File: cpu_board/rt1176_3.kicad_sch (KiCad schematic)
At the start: 19 parts

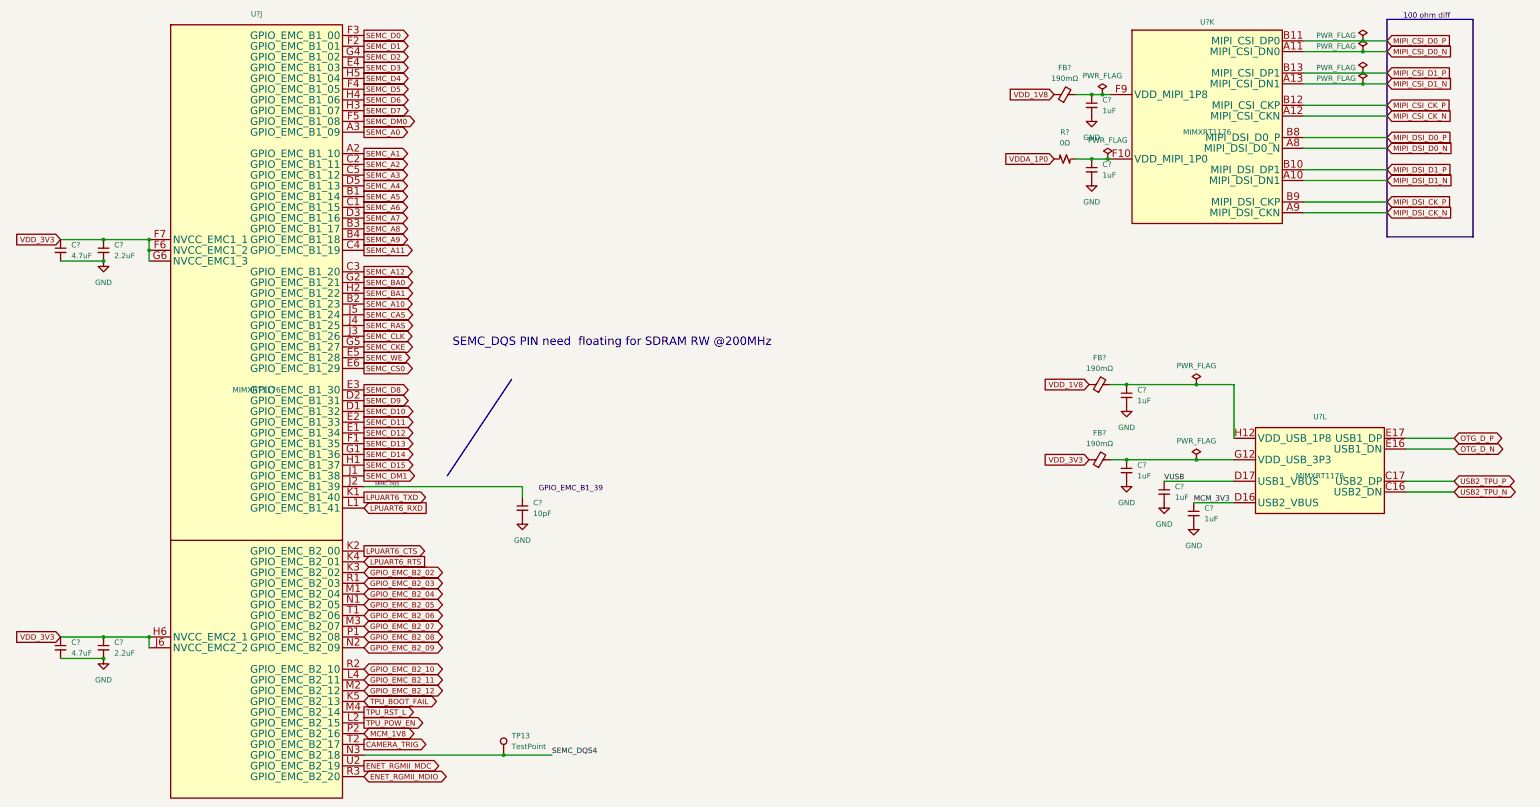
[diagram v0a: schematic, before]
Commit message: clean up board2board connector and organize TODOs
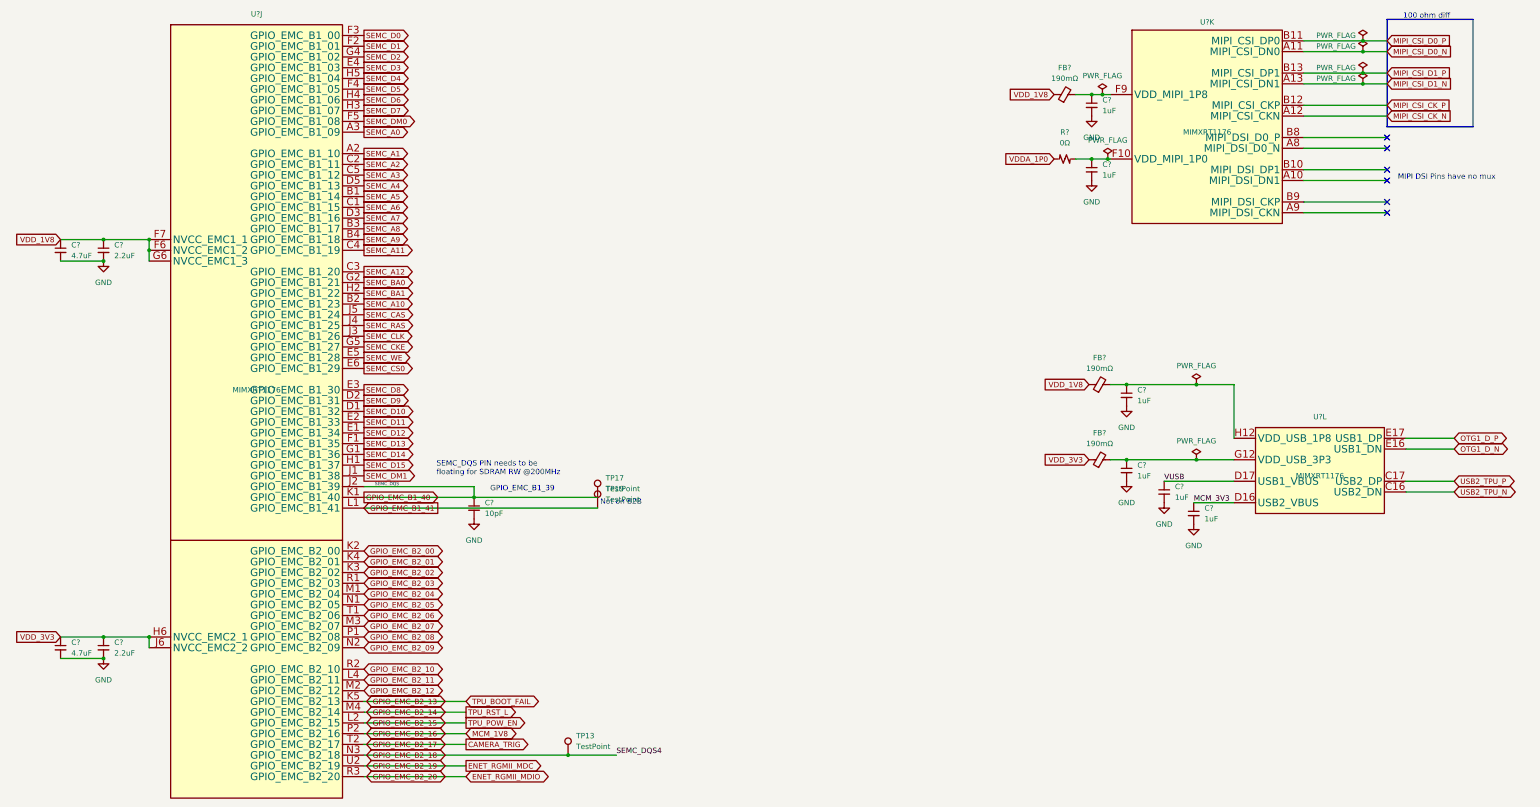
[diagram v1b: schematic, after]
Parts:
- added TP17, TP19: TestPoint, TestPoint:TestPoint_Pad_1.5x1.5mm, symbol Connector:TestPoint
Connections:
- net LPUART6_TXD is gone; now on net GPIO_EMC_B1_40: U?.K1 (GPIO_EMC_B1_40)
- net VDD_1V8: now also C?.1, C?.1, U?.F6 (NVCC_EMC1_2), U?.F7 (NVCC_EMC1_1), U?.G6 (NVCC_EMC1_3)
- net VDD_3V3: no longer C?.1, C?.1, U?.F6 (NVCC_EMC1_2), U?.F7 (NVCC_EMC1_1), U?.G6 (NVCC_EMC1_3)
- net GPIO_EMC_B1_40: now reaches C?.1, U?.J2 (GPIO_EMC_B1_39)
- net GPIO_EMC_B1_40: now also TP17.1
- net LPUART6_CTS renamed GPIO_EMC_B2_00
- net LPUART6_RTS renamed GPIO_EMC_B2_01
- net LPUART6_RXD renamed GPIO_EMC_B1_41
- net GPIO_EMC_B1_41: now also TP19.1
- net MCM_1V8 renamed GPIO_EMC_B2_16
- net MIPI_DSI_CK_N: no longer names the net of U?.A9 (MIPI_DSI_CKN)
- net MIPI_DSI_CK_P: no longer names the net of U?.B9 (MIPI_DSI_CKP)
- net MIPI_DSI_D0_N: no longer names the net of U?.A8 (MIPI_DSI_D0_N)
- net MIPI_DSI_D0_P: no longer names the net of U?.B8 (MIPI_DSI_D0_P)
- net MIPI_DSI_D1_N: no longer names the net of U?.A10 (MIPI_DSI_DN1)
- net MIPI_DSI_D1_P: no longer names the net of U?.B10 (MIPI_DSI_DP1)
- net OTG_D_N renamed OTG1_D_N
- net OTG_D_P renamed OTG1_D_P
- net SEMC_DQS4 renamed GPIO_EMC_B2_18
- net TPU_BOOT_FAIL renamed GPIO_EMC_B2_13
- net TPU_POW_EN renamed GPIO_EMC_B2_15
- net TPU_RST_L renamed GPIO_EMC_B2_14
- no-connect marks 0 -> 6
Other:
- note added: "MIPI DSI Pins have no mux"
- note added: "Not on B2B"
- note added: "SEMC_DQS PIN needs to be floating for SDRAM RW @200MHz"
- note removed: "SEMC_DQS PIN need floating for SDRAM RW @200MHz"
- moved on the sheet: C?, TP13

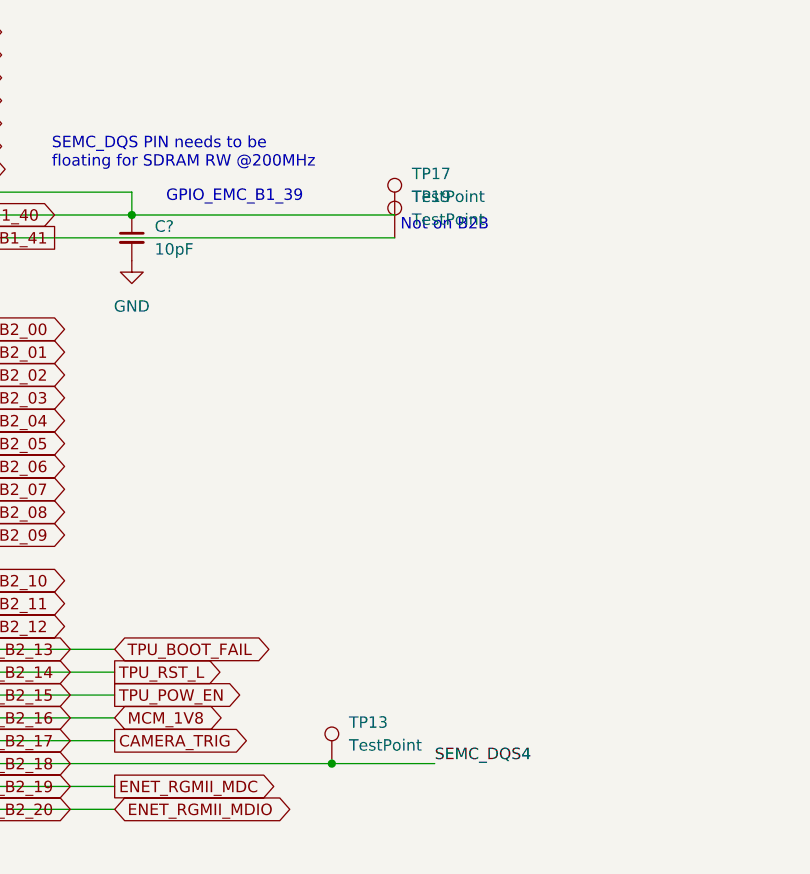
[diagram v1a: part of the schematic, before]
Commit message: route most of power distribution
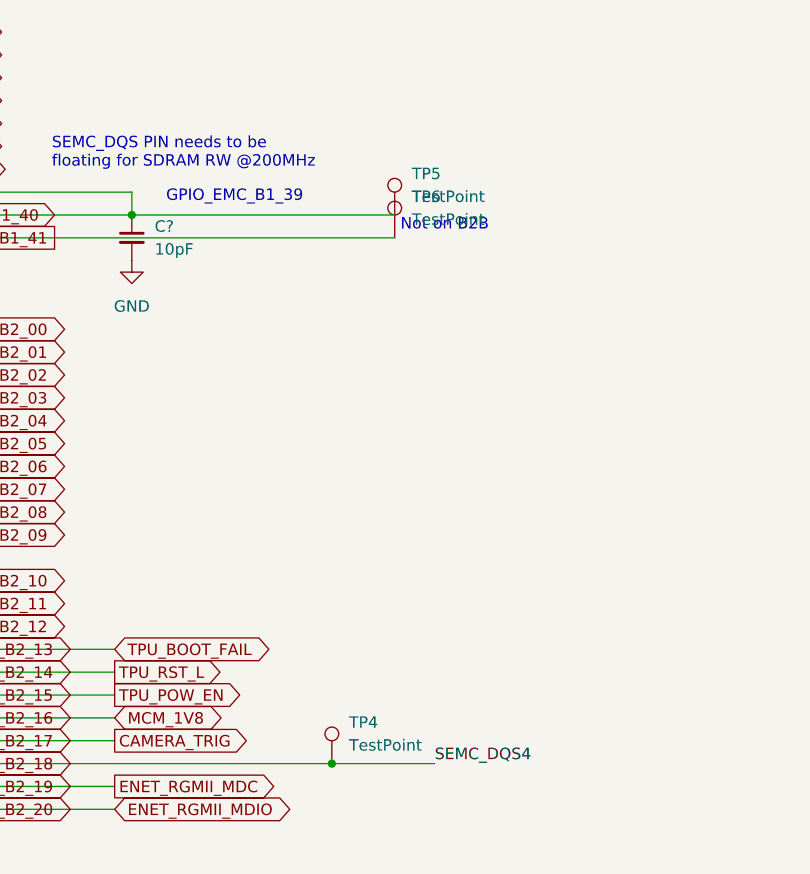
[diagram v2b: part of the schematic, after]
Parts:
- TP4: renamed from TP13; footprint TestPoint:TestPoint_Pad_1.5x1.5mm -> TestPoint:TestPoint_Pad_1.0x1.0mm; JLCPCB P/N (none) -> C221678
- TP5: renamed from TP17; footprint TestPoint:TestPoint_Pad_1.5x1.5mm -> TestPoint:TestPoint_Pad_1.0x1.0mm; JLCPCB P/N (none) -> C221678
- TP6: renamed from TP19; footprint TestPoint:TestPoint_Pad_1.5x1.5mm -> TestPoint:TestPoint_Pad_1.0x1.0mm; JLCPCB P/N (none) -> C221678

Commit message: floorplan complete
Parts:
- removed C?: 1uF, Capacitor_SMD:C_0402_1005Metric, symbol Device:C_Small
- removed C?: 10pF, Capacitor_SMD:C_0402_1005Metric, symbol Device:C_Small
- removed R?: 0Ω, Resistor_SMD:R_0402_1005Metric, symbol Device:R_Small_US
- removed TP4, TP5, TP6: TestPoint, TestPoint:TestPoint_Pad_1.0x1.0mm, symbol Connector:TestPoint
- added C?: 10pF, Capacitor_SMD:C_0402_1005Metric, symbol Device:C_Small
- added R?: 10kΩ, Resistor_SMD:R_0402_1005Metric, symbol Device:R_Small_US
- FB? (x3): footprint adcs:L0402_H0.55MM -> Inductor_SMD:L_0402_1005Metric
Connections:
- net GND: now also C?.2, R?.1
- net GPIO_EMC_B1_40: no longer U?.J2 (GPIO_EMC_B1_39)
- net VDD_USB_3P3: now reaches C?.1, FB?.2, U?.G12 (VDD_USB_3P3)
- net VDD_USB_1P8: now reaches C?.1, FB?.2, U?.H12 (VDD_USB_1P8)
- net VDD_MIPI_1P0: now reaches U?.F10 (VDD_MIPI_1P0)
- net VDD_MIPI_1P0: now also R?.2
- new net SEMC_DQS: C?.1, U?.J2 (GPIO_EMC_B1_39)
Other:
- note added: "Per HDUG, 10k resistor to ground recommended when not in use"
- note removed: "GPIO_EMC_B1_39"
- note removed: "Not on B2B"
- note removed: "SEMC_DQS"

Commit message: add models and power diagram
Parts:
- U? (x3): footprint adcs:BGA289C80P17X17_1400X14000X152 -> adcs:U_MIMXRT1176DVMAA_NXP
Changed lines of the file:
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@@
       (effects (font (size 1.27 1.27)))
     )
-    (property "Footprint" "adcs:BGA289C80P17X17_1400X14000X152" (at 314.96 83.185 0)
+    (property "Footprint" "adcs:U_MIMXRT1176DVMAA_NXP" (at 314.96 83.185 0)
       (effects (font (size 1.27 1.27)) hide)
     )
@@
     (property "Footprint (for JLCPCB)" "" (at 314.96 81.915 0)
       (effects (font (size 1.27 1.27)) hide)
+    )
+    (property "DigiKey Part Number" "" (at 314.96 81.915 0)
+      (effects (font (size 1.27 1.27)) hide)
+    )
+    (property "Tolerance" "" (at 314.96 81.915 0)
+      (effects (font (size 1.27 1.27)))
+    )
+    (property "Power Rating" "" (at 314.96 81.915 0)
+      (effects (font (size 1.27 1.27)))
     )
     (pin "L9")
@@
       (effects (font (size 1.27 1.27)))
     )
-    (property "Footprint" "adcs:BGA289C80P17X17_1400X14000X152" (at 90.17 144.145 0)
+    (property "Footprint" "adcs:U_MIMXRT1176DVMAA_NXP" (at 90.17 144.145 0)
       (effects (font (size 1.27 1.27)) hide)
     )
@@
     (property "Footprint (for JLCPCB)" "" (at 90.17 142.875 0)
       (effects (font (size 1.27 1.27)) hide)
+    )
+    (property "DigiKey Part Number" "" (at 90.17 142.875 0)
+      (effects (font (size 1.27 1.27)) hide)
+    )
+    (property "Tolerance" "" (at 90.17 142.875 0)
+      (effects (font (size 1.27 1.27)))
+    )
+    (property "Power Rating" "" (at 90.17 142.875 0)
+      (effects (font (size 1.27 1.27)))
     )
     (pin "L9")
@@
       (effects (font (size 1.27 1.27)))
     )
-    (property "Footprint" "adcs:BGA289C80P17X17_1400X14000X152" (at 341.63 164.465 0)
+    (property "Footprint" "adcs:U_MIMXRT1176DVMAA_NXP" (at 341.63 164.465 0)
       (effects (font (size 1.27 1.27)) hide)
     )
@@
       (effects (font (size 1.27 1.27)) hide)
     )
+    (property "DigiKey Part Number" "" (at 341.63 163.195 0)
+      (effects (font (size 1.27 1.27)) hide)
+    )
+    (property "Tolerance" "" (at 341.63 163.195 0)
+      (effects (font (size 1.27 1.27)))
+    )
+    (property "Power Rating" "" (at 341.63 163.195 0)
+      (effects (font (size 1.27 1.27)))
+    )
     (pin "L9")

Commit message: continue work on fanout
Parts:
- removed FB? (x2): 190mΩ, Inductor_SMD:L_0402_1005Metric, symbol Device:FerriteBead_Small
- C? (x9): footprint Capacitor_SMD:C_0402_1005Metric -> adcs:Perfect_0201
- C?: footprint Capacitor_SMD:C_0402_1005Metric -> adcs:Perfect_0402
- FB?: footprint Inductor_SMD:L_0402_1005Metric -> adcs:Perfect_0402
- R?: footprint Resistor_SMD:R_0402_1005Metric -> adcs:Perfect_0201
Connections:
- net VDD_USB_1P8 is gone; now on net VDD_1V8: C?.1, U?.H12 (VDD_USB_1P8)
- net VDD_USB_3P3 is gone; now on net VDD_3V3: C?.1, U?.G12 (VDD_USB_3P3)
- net MIPI_CSI_CK_N: no longer names the net of U?.A12 (MIPI_CSI_CKN)
- net MIPI_CSI_CK_P: no longer names the net of U?.B12 (MIPI_CSI_CKP)
- net MIPI_CSI_D0_N: no longer names the net of U?.A11 (MIPI_CSI_DN0)
- net MIPI_CSI_D0_P: no longer names the net of U?.B11 (MIPI_CSI_DP0)
- net MIPI_CSI_D1_N: no longer names the net of U?.A13 (MIPI_CSI_DN1)
- net MIPI_CSI_D1_P: no longer names the net of U?.B13 (MIPI_CSI_DP1)
- net USB2_TPU_N: no longer names the net of U?.C16 (USB2_DN)
- net USB2_TPU_P: no longer names the net of U?.C17 (USB2_DP)
- no-connect marks 6 -> 14
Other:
- note added: "Do I need to power this if we are not using the OTGs?"
- note added: "MIPI_CSI_CK_N"
- note added: "MIPI_CSI_CK_P"
- note added: "MIPI_CSI_D0_N"
- note added: "MIPI_CSI_D0_P"
- note added: "MIPI_CSI_D1_N"
- note added: "MIPI_CSI_D1_P"
- note added: "Removed ferrite beads here!"

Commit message: clean up silkscreen
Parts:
- C? (x9), R?: Footprint (for JLCPCB) 0402 -> 0201
- FB?: Footprint (for JLCPCB) (none) -> 0401
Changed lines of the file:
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@@
       (effects (font (size 1.27 1.27)) hide)
     )
-    (property "Footprint (for JLCPCB)" "0402" (at 43.815 111.125 0)
+    (property "Footprint (for JLCPCB)" "0201" (at 43.815 111.125 0)
       (effects (font (size 1.27 1.27)) hide)
     )
@@
       (effects (font (size 1.27 1.27)) hide)
     )
-    (property "Footprint (for JLCPCB)" "0402" (at 43.815 205.105 0)
+    (property "Footprint (for JLCPCB)" "0201" (at 43.815 205.105 0)
       (effects (font (size 1.27 1.27)) hide)
     )
@@
       (effects (font (size 1.27 1.27)) hide)
     )
-    (property "Footprint (for JLCPCB)" "0402" (at 177.165 170.18 0)
+    (property "Footprint (for JLCPCB)" "0201" (at 177.165 170.18 0)
       (effects (font (size 1.27 1.27)) hide)
     )
@@
       (effects (font (size 1.27 1.27)) hide)
     )
-    (property "Datasheet" "~" (at 281.305 74.295 0)
+    (property "Datasheet" "" (at 281.305 74.295 0)
       (effects (font (size 1.27 1.27)) hide)
     )
@@
       (effects (font (size 1.27 1.27)) hide)
     )
-    (property "Footprint (for JLCPCB)" "" (at 281.305 74.295 0)
+    (property "Footprint (for JLCPCB)" "0401" (at 281.305 74.295 0)
       (effects (font (size 1.27 1.27)) hide)
     )
@@
       (effects (font (size 1.27 1.27)) hide)
     )
-    (property "Footprint (for JLCPCB)" "0402" (at 287.655 76.835 0)
+    (property "Footprint (for JLCPCB)" "0201" (at 287.655 76.835 0)
       (effects (font (size 1.27 1.27)) hide)
     )
@@
       (effects (font (size 1.27 1.27)) hide)
     )
-    (property "Datasheet" "~" (at 53.975 111.125 0)
+    (property "Datasheet" "" (at 53.975 111.125 0)
       (effects (font (size 1.27 1.27)) hide)
     )
@@
       (effects (font (size 1.27 1.27)) hide)
     )
-    (property "Footprint (for JLCPCB)" "0402" (at 53.975 111.125 0)
+    (property "Footprint (for JLCPCB)" "0201" (at 53.975 111.125 0)
       (effects (font (size 1.27 1.27)) hide)
     )
@@
       (effects (font (size 1.27 1.27)) hide)
     )
-    (property "Footprint (for JLCPCB)" "0402" (at 311.785 173.355 0)
+    (property "Footprint (for JLCPCB)" "0201" (at 311.785 173.355 0)
       (effects (font (size 1.27 1.27)) hide)
     )
@@
       (effects (font (size 1.27 1.27)) hide)
     )
-    (property "Datasheet" "~" (at 53.975 205.105 0)
+    (property "Datasheet" "" (at 53.975 205.105 0)
       (effects (font (size 1.27 1.27)) hide)
     )
@@
       (effects (font (size 1.27 1.27)) hide)
     )
-    (property "Footprint (for JLCPCB)" "0402" (at 53.975 205.105 0)
+    (property "Footprint (for JLCPCB)" "0201" (at 53.975 205.105 0)
       (effects (font (size 1.27 1.27)) hide)
     )
@@
       (effects (font (size 1.27 1.27)) hide)
     )
-    (property "Footprint (for JLCPCB)" "0402" (at 291.465 92.075 0)
+    (property "Footprint (for JLCPCB)" "0201" (at 291.465 92.075 0)
       (effects (font (size 1.27 1.27)) hide)
     )
@@
       (effects (font (size 1.27 1.27)) hide)
     )
-    (property "Footprint (for JLCPCB)" "0402" (at 295.91 145.415 0)
+    (property "Footprint (for JLCPCB)" "0201" (at 295.91 145.415 0)
       (effects (font (size 1.27 1.27)) hide)
     )
@@
       (effects (font (size 1.27 1.27)) hide)
     )
-    (property "Footprint (for JLCPCB)" "0402" (at 295.91 163.195 0)
-      (effects (font (size 1.27 1.27)) hide)
-    )
+    (property "Footprint (for JLCPCB)" "0201" (at 295.91 163.195 0)
+      (effects (font (size 1.27 1.27)) hide)
+    )

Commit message: soldermander 1.0 ready for review
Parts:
- C? (x2): Voltage Rating (none) -> 6.3V
- C? (x2): Voltage Rating (none) -> 50V
- C? (x6): Voltage Rating (none) -> 10V
- R?: JLCPCB P/N (none) -> C3152014
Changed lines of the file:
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@@
       (effects (font (size 1.27 1.27)))
+    )
+    (property "Voltage Rating" "6.3V" (at 43.815 111.125 0)
+      (effects (font (size 1.27 1.27)) hide)
     )
     (pin "1")
@@
       (effects (font (size 1.27 1.27)))
     )
+    (property "Voltage Rating" "6.3V" (at 43.815 205.105 0)
+      (effects (font (size 1.27 1.27)) hide)
+    )
     (pin "1")
     (pin "2")
@@
       (effects (font (size 1.27 1.27)) hide)
     )
+    (property "Voltage Rating" "50V" (at 177.165 170.18 0)
+      (effects (font (size 1.27 1.27)) hide)
+    )
     (pin "1")
     (pin "2")
@@
       (effects (font (size 1.27 1.27)) hide)
     )
+    (property "Voltage Rating" "10V" (at 287.655 76.835 0)
+      (effects (font (size 1.27 1.27)) hide)
+    )
     (pin "1")
     (pin "2")
@@
       (effects (font (size 1.27 1.27)) hide)
     )
+    (property "Voltage Rating" "10V" (at 53.975 111.125 0)
+      (effects (font (size 1.27 1.27)) hide)
+    )
     (pin "1")
     (pin "2")
@@
       (effects (font (size 1.27 1.27)) hide)
     )
+    (property "Voltage Rating" "10V" (at 311.785 173.355 0)
+      (effects (font (size 1.27 1.27)) hide)
+    )
     (pin "1")
     (pin "2")
@@
     )
     (property "Footprint (for JLCPCB)" "0201" (at 53.975 205.105 0)
+      (effects (font (size 1.27 1.27)) hide)
+    )
+    (property "Voltage Rating" "10V" (at 53.975 205.105 0)
       (effects (font (size 1.27 1.27)) hide)
     )
@@
       (effects (font (size 1.27 1.27)))
     )
+    (property "Voltage Rating" "50V" (at 304.8 168.275 0)
+      (effects (font (size 1.27 1.27)) hide)
+    )
     (pin "1")
     (pin "2")
@@
       (effects (font (size 1.27 1.27)) hide)
     )
-    (property "JLCPCB P/N" "" (at 291.465 92.075 0)
+    (property "JLCPCB P/N" "C3152014" (at 291.465 92.075 0)
       (effects (font (size 1.27 1.27)) hide)
     )
@@
     )
     (property "Footprint (for JLCPCB)" "0201" (at 295.91 145.415 0)
+      (effects (font (size 1.27 1.27)) hide)
+    )
+    (property "Voltage Rating" "10V" (at 295.91 145.415 0)
       (effects (font (size 1.27 1.27)) hide)
     )
@@
       (effects (font (size 1.27 1.27)) hide)
     )
+    (property "Voltage Rating" "10V" (at 295.91 163.195 0)
+      (effects (font (size 1.27 1.27)) hide)
+    )

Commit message: update
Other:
- company: (none) -> Stanford Student Space Initiative
- title: (none) -> Soldermander
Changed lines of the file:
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@@
 (kicad_sch (version 20230121) (generator eeschema)
   (paper "A3")
+  (title_block
+    (title "Soldermander")
+    (date "2024-02-27")
+    (rev "1.0")
+    (company "Stanford Student Space Initiative")
+    (comment 1 "RE: Flynn Dreilinger")
+  )
   (junction (at 351.79 64.135) (diameter 0) (color 0 0 0 0)
   )
